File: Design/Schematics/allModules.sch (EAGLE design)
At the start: 196 parts, among them IC1 MAX7219CNG, IC2 MAX7219CNG, IC3 MAX7219CNG, IC4 MAX7219CNG, IC5 MCP3008, SW1 arcade_btn, SW2 arcade_btn, SW3 arcade_btn, SW4 arcade_btn, U1 328P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

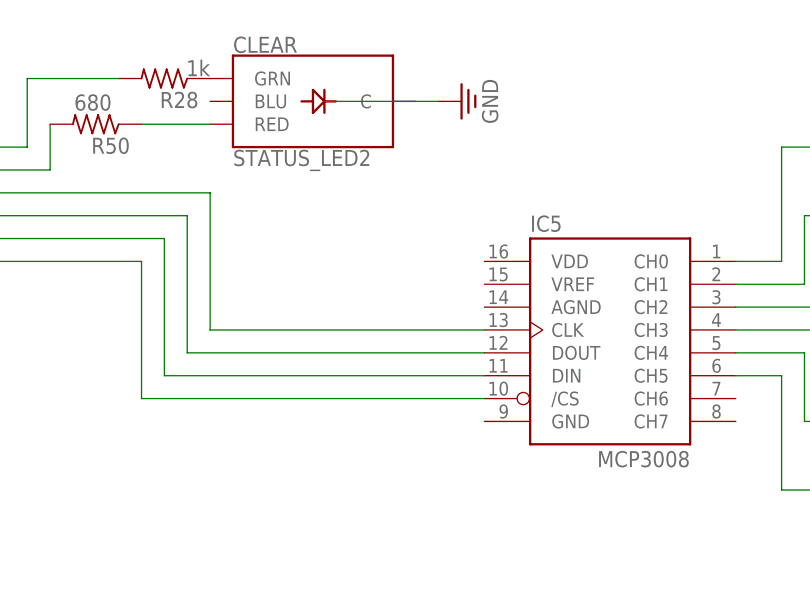
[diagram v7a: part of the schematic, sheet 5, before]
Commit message: Added power connections for wires module
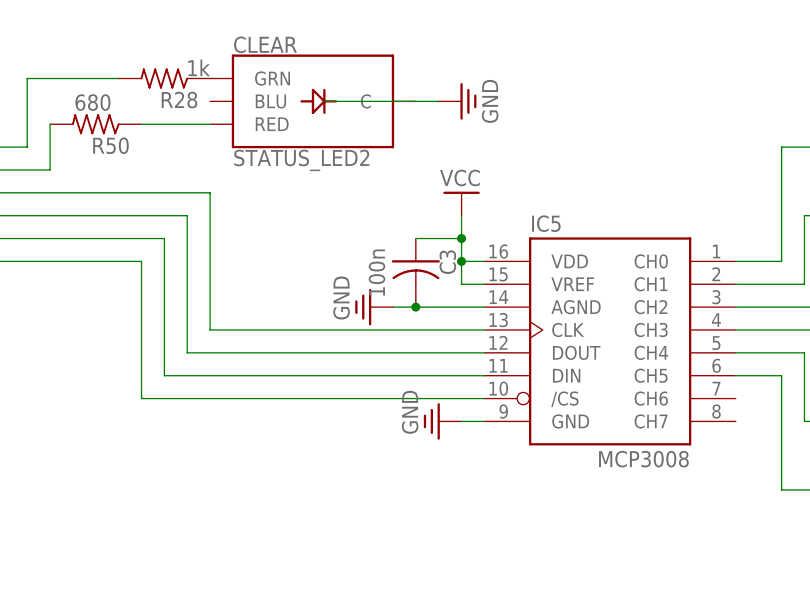
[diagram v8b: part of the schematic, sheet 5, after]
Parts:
- added C3: 100n, adafruit:C-US025-024X044
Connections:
- net GND: now also C3.2, IC5.AGND, IC5.GND
- net VCC: now also C3.1, IC5.VDD, IC5.VREF
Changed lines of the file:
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@@
 <part name="SUPPLY46" library="Power_Symbols" library_urn="urn:adsk.eagle:library:16502351" deviceset="GND-EARTH" device="" value="GND"/>
 <part name="IC5" library="adafruit" library_urn="urn:adsk.eagle:library:420" deviceset="MCP3008" device="" package3d_urn="urn:adsk.eagle:package:6240922/1"/>
+<part name="SUPPLY47" library="Power_Symbols" library_urn="urn:adsk.eagle:library:16502351" deviceset="GND-EARTH" device="" value="GND"/>
+<part name="SUPPLY48" library="Power_Symbols" library_urn="urn:adsk.eagle:library:16502351" deviceset="GND-EARTH" device="" value="GND"/>
+<part name="VCC27" library="m-pad-2.1" deviceset="VCC" device=""/>
+<part name="C3" library="adafruit" library_urn="urn:adsk.eagle:library:420" deviceset="C-US" device="025-024X044" package3d_urn="urn:adsk.eagle:package:6240324/1" value="100n"/>
 </parts>
 <sheets>
@@
 <attribute name="NAME" x="27.94" y="7.62" size="1.778" layer="95" rot="MR180"/>
 </instance>
+<instance part="SUPPLY47" gate="G$1" x="10.16" y="-2.54" smashed="yes" rot="MR90">
+<attribute name="VALUE" x="6.985" y="-1.524" size="1.778" layer="96" rot="MR90" align="center"/>
+</instance>
+<instance part="SUPPLY48" gate="G$1" x="17.78" y="-15.24" smashed="yes" rot="MR90">
+<attribute name="VALUE" x="14.605" y="-14.224" size="1.778" layer="96" rot="MR90" align="center"/>
+</instance>
+<instance part="VCC27" gate="1" x="20.32" y="7.62" smashed="yes" rot="MR0">
+<attribute name="VALUE" x="22.479" y="10.922" size="1.778" layer="96" rot="MR0"/>
+</instance>
+<instance part="C3" gate="G$1" x="15.24" y="2.54" smashed="yes">
+<attribute name="NAME" x="19.685" y="1.016" size="1.778" layer="95" rot="R90"/>
+<attribute name="VALUE" x="11.811" y="-1.524" size="1.778" layer="96" rot="R90"/>
+</instance>
 </instances>
 <busses>
@@
 <wire x1="-78.74" y1="-60.96" x2="-76.2" y2="-60.96" width="0.1524" layer="91"/>
 <label x="-76.2" y="-60.96" size="1.778" layer="95"/>
+</segment>
+<segment>
+<pinref part="SUPPLY47" gate="G$1" pin="GND"/>
+<pinref part="IC5" gate="G$1" pin="AGND"/>
+<wire x1="12.7" y1="-2.54" x2="15.24" y2="-2.54" width="0.1524" layer="91"/>
+<pinref part="C3" gate="G$1" pin="2"/>
+<wire x1="15.24" y1="-2.54" x2="22.86" y2="-2.54" width="0.1524" layer="91"/>
+<junction x="15.24" y="-2.54"/>
+</segment>
+<segment>
+<pinref part="SUPPLY48" gate="G$1" pin="GND"/>
+<pinref part="IC5" gate="G$1" pin="GND"/>
+<wire x1="20.32" y1="-15.24" x2="22.86" y2="-15.24" width="0.1524" layer="91"/>
 </segment>
 </net>
@@
 <pinref part="VCC22" gate="1" pin="VCC"/>
 </segment>
-</net>
+<segment>
+<pinref part="VCC27" gate="1" pin="VCC"/>
+<wire x1="20.32" y1="7.62" x2="20.32" y2="5.08" width="0.1524" layer="91"/>
+<pinref part="IC5" gate="G$1" pin="VDD"/>
+<wire x1="20.32" y1="5.08" x2="20.32" y2="2.54" width="0.1524" layer="91"/>
+<wire x1="20.32" y1="2.54" x2="22.86" y2="2.54" width="0.1524" layer="91"/>
+<pinref part="IC5" gate="G$1" pin="VREF"/>
+<wire x1="22.86" y1="0" x2="20.32" y2="0" width="0.1524" layer="91"/>
+<wire x1="20.32" y1="0" x2="20.32" y2="2.54" width="0.1524" layer="91"/>
+<junction x="20.32" y="2.54"/>
+<pinref part="C3" gate="G$1" pin="1"/>
+<wire x1="15.24" y1="5.08" x2="20.32" y2="5.08" width="0.1524" layer="91"/>
+<junction x="20.32" y="5.08"/>
+</segment>
+</net>
